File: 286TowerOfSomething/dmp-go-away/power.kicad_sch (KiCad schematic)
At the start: 1 part, among them U1 M6117C

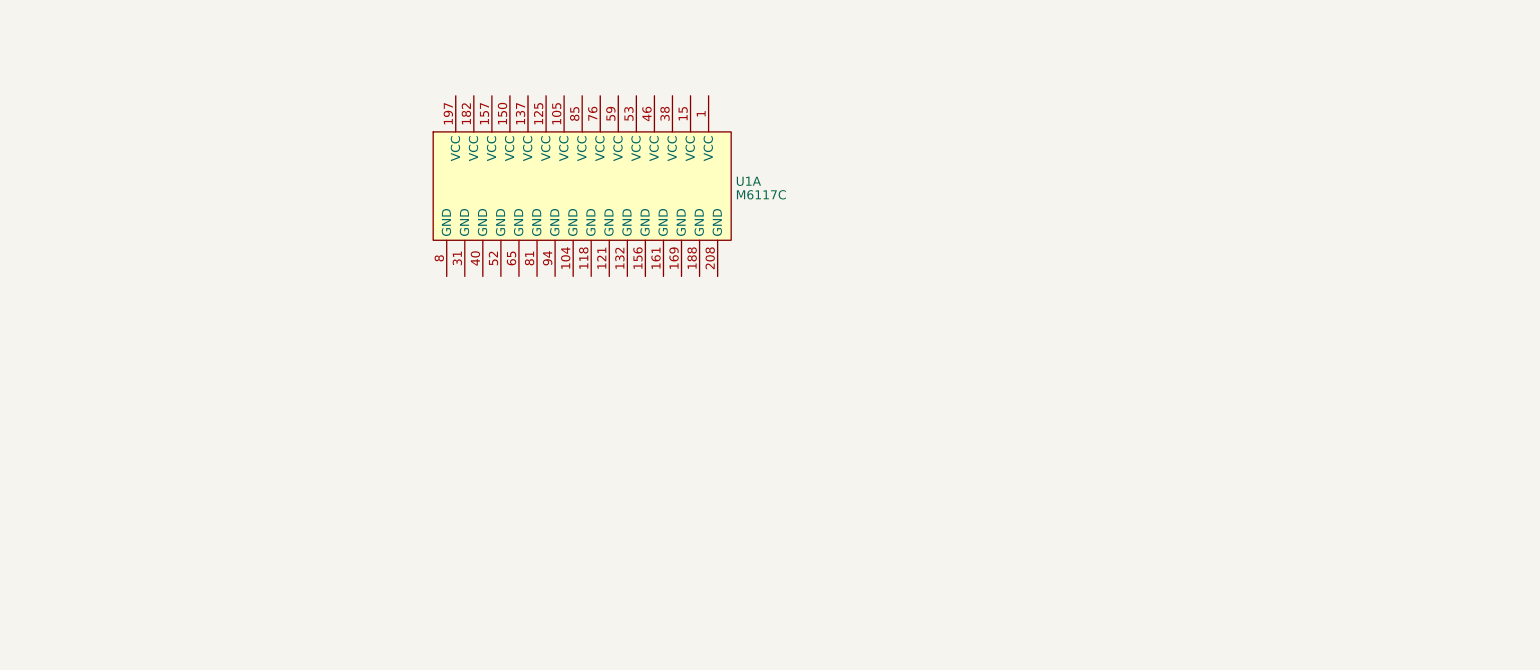
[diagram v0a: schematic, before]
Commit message: Adding work done on 386 card, coming along nicely
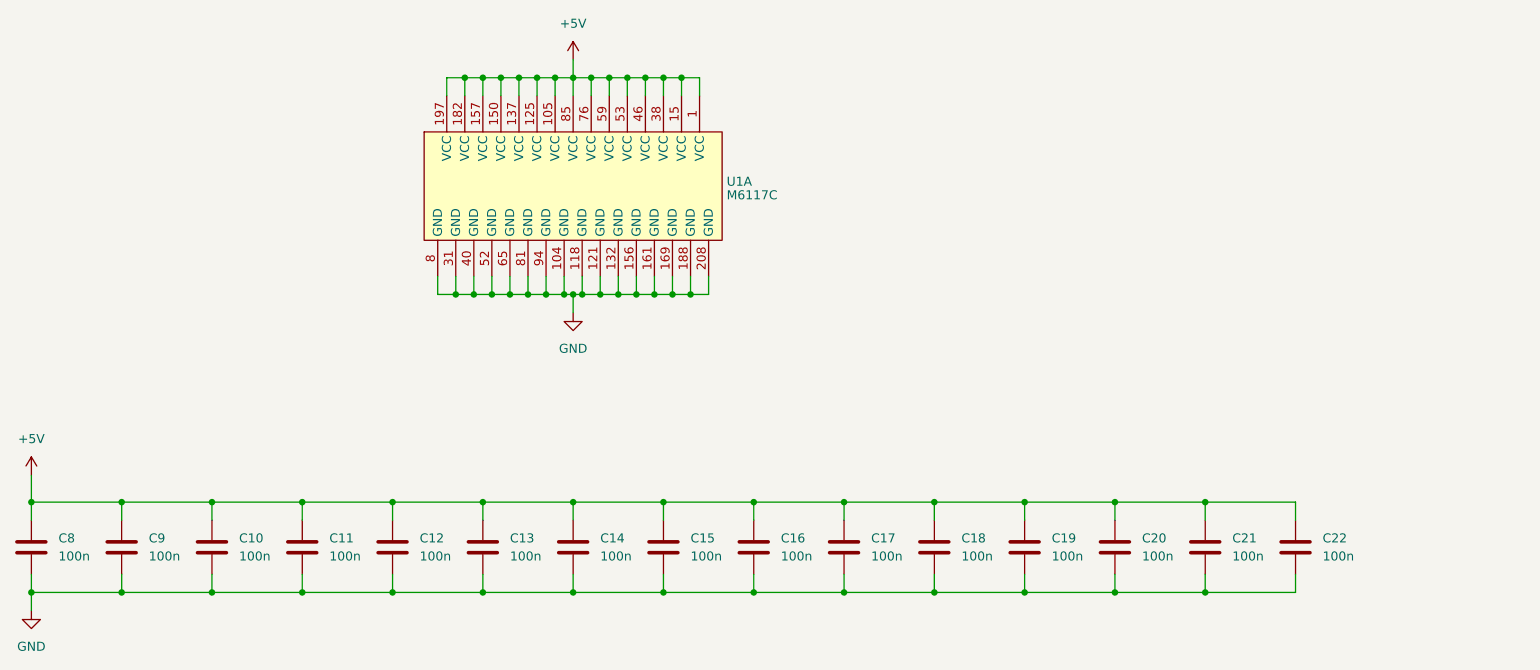
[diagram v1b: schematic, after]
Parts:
- added C10, C11, C12, C13, C14, C15, C16, C17, C18, C19, C20, C21, C22, C8, C9: 100n, symbol Device:C
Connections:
- net +5V: now reaches U1.1 (VCC)
- net +5V: now also U1.105 (VCC), U1.125 (VCC), U1.137 (VCC), U1.15 (VCC), U1.150 (VCC), U1.157 (VCC), U1.182 (VCC), U1.197 (VCC), U1.38 (VCC), U1.46 (VCC), U1.53 (VCC), U1.59 (VCC), U1.76 (VCC), U1.85 (VCC), C10.1, C11.1, C12.1, C13.1, C14.1, C15.1, C16.1, C17.1, C18.1, C19.1, C20.1, C21.1, C22.1, C8.1, C9.1
- net GND: now reaches U1.104 (GND)
- net GND: now also U1.118 (GND), U1.121 (GND), U1.132 (GND), U1.156 (GND), U1.161 (GND), U1.169 (GND), U1.188 (GND), U1.208 (GND), U1.31 (GND), U1.40 (GND), U1.52 (GND), U1.65 (GND), U1.8 (GND), U1.81 (GND), U1.94 (GND), C10.2, C11.2, C12.2, C13.2, C14.2, C15.2, C16.2, C17.2, C18.2, C19.2, C20.2, C21.2, C22.2, C8.2, C9.2
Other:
- moved on the sheet: U1A

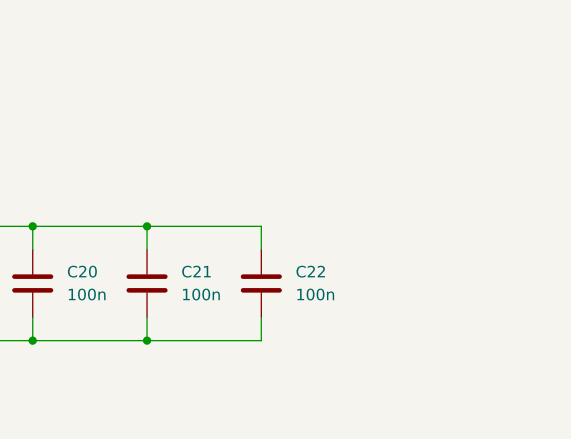
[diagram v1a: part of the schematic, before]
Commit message: Adding some missing caps, and the optional DS12885 RTC for dmp-go-away
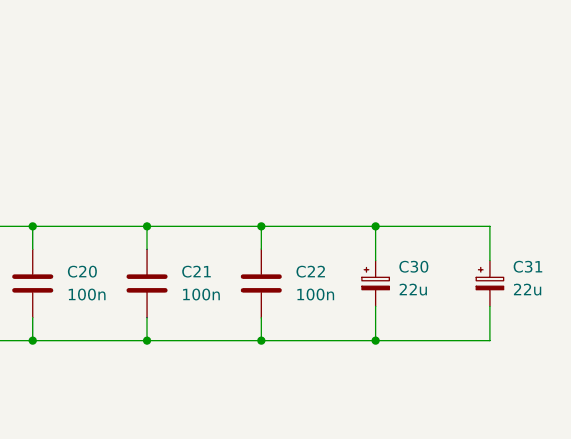
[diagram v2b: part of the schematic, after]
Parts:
- added C30, C31: 22u, symbol Device:C_Polarized_Small
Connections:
- net +5V: now also C30.1, C31.1
- net GND: now also C30.2, C31.2
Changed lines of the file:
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@@
 	(paper "USLetter")
 	(junction
+		(at 228.6 158.75)
+		(diameter 0)
+		(color 0 0 0 0)
+	)
+	(junction
 		(at 127 146.05)
 		(diameter 0)
@@
 	)
 	(junction
+		(at 241.3 146.05)
+		(diameter 0)
+		(color 0 0 0 0)
+	)
+	(junction
 		(at 76.2 158.75)
 		(diameter 0)
@@
 	)
 	(junction
+		(at 228.6 146.05)
+		(diameter 0)
+		(color 0 0 0 0)
+	)
+	(junction
 		(at 114.3 146.05)
 		(diameter 0)
@@
 	)
 	(junction
+		(at 241.3 158.75)
+		(diameter 0)
+		(color 0 0 0 0)
+	)
+	(junction
 		(at 129.54 86.36)
 		(diameter 0)
@@
 	(wire
 		(pts
+			(xy 241.3 146.05) (xy 228.6 146.05)
+		)
+		(stroke
+			(width 0)
+			(type default)
+		)
+	)
+	(wire
+		(pts
 			(xy 228.6 158.75) (xy 228.6 156.21)
 		)
@@
 	(wire
 		(pts
+			(xy 228.6 158.75) (xy 241.3 158.75)
+		)
+		(stroke
+			(width 0)
+			(type default)
+		)
+	)
+	(wire
+		(pts
 			(xy 165.1 156.21) (xy 165.1 158.75)
 		)
@@
 	(wire
 		(pts
+			(xy 254 146.05) (xy 241.3 146.05)
+		)
+		(stroke
+			(width 0)
+			(type default)
+		)
+	)
+	(wire
+		(pts
 			(xy 130.81 114.3) (xy 130.81 116.84)
 		)
@@
 	(wire
 		(pts
+			(xy 241.3 149.86) (xy 241.3 146.05)
+		)
+		(stroke
+			(width 0)
+			(type default)
+		)
+	)
+	(wire
+		(pts
 			(xy 109.22 88.9) (xy 109.22 86.36)
 		)
@@
 	(wire
 		(pts
+			(xy 241.3 158.75) (xy 254 158.75)
+		)
+		(stroke
+			(width 0)
+			(type default)
+		)
+	)
+	(wire
+		(pts
 			(xy 139.7 146.05) (xy 152.4 146.05)
 		)
@@
 	(wire
 		(pts
+			(xy 241.3 158.75) (xy 241.3 154.94)
+		)
+		(stroke
+			(width 0)
+			(type default)
+		)
+	)
+	(wire
+		(pts
 			(xy 127 86.36) (xy 129.54 86.36)
 		)
@@
 	(wire
 		(pts
+			(xy 254 149.86) (xy 254 146.05)
+		)
+		(stroke
+			(width 0)
+			(type default)
+		)
+	)
+	(wire
+		(pts
 			(xy 110.49 114.3) (xy 110.49 116.84)
 		)
@@
 	(wire
 		(pts
+			(xy 254 154.94) (xy 254 158.75)
+		)
+		(stroke
+			(width 0)
+			(type default)
+		)
+	)
+	(wire
+		(pts
 			(xy 119.38 86.36) (xy 119.38 88.9)
 		)
@@
 	)
 	(symbol
+		(lib_id "Device:C_Polarized_Small")
+		(at 241.3 152.4 0)
+		(unit 1)
+		(exclude_from_sim no)
+		(in_bom yes)
+		(on_board yes)
+		(dnp no)
+		(fields_autoplaced yes)
+		(property "Reference" "C30"
+			(at 243.84 150.5838 0)
+			(effects
+				(font
+					(size 1.27 1.27)
+				)
+				(justify left)
+			)
+		)
+		(property "Value" "22u"
+			(at 243.84 153.1238 0)
+			(effects
+				(font
+					(size 1.27 1.27)
+				)
+				(justify left)
+			)
+		)
+		(property "Footprint" ""
+			(at 241.3 152.4 0)
+			(effects
+				(font
+					(size 1.27 1.27)
+				)
+				(hide yes)
+			)
+		)
+		(property "Datasheet" "~"
+			(at 241.3 152.4 0)
+			(effects
+				(font
+					(size 1.27 1.27)
+				)
+				(hide yes)
+			)
+		)
+		(property "Description" "Polarized capacitor, small symbol"
+			(at 241.3 152.4 0)
+			(effects
+				(font
+					(size 1.27 1.27)
+				)
+				(hide yes)
+			)
+		)
+		(pin "2"
+		)
+		(pin "1"
+		)
+		(instances
+			(project ""
+				(path "/b66cfc40-8652-41e7-bd5f-f23cb0cb78db/de3f85e5-98cb-47f6-9751-2a5a4919266b"
+					(reference "C30")
+					(unit 1)
+				)
+			)
+		)
+	)
+	(symbol
 		(lib_id "power:+5V")
 		(at 127 83.82 0)
@@
 					(unit 1)
 				)
+			)
+		)
+	)
+	(symbol
+		(lib_id "Device:C_Polarized_Small")
+		(at 254 152.4 0)
+		(unit 1)
+		(exclude_from_sim no)
+		(in_bom yes)
+		(on_board yes)
+		(dnp no)
+		(fields_autoplaced yes)
+		(property "Reference" "C31"
+			(at 256.54 150.5838 0)
+			(effects
+				(font
+					(size 1.27 1.27)
+				)
+				(justify left)
+			)
+		)
+		(property "Value" "22u"
+			(at 256.54 153.1238 0)
+			(effects
+				(font
+					(size 1.27 1.27)
+				)
+				(justify left)
+			)
+		)
+		(property "Footprint" ""
+			(at 254 152.4 0)
+			(effects
+				(font
+					(size 1.27 1.27)
+				)
+				(hide yes)
+			)
+		)
+		(property "Datasheet" "~"
+			(at 254 152.4 0)
+			(effects
+				(font
+					(size 1.27 1.27)
+				)
+				(hide yes)
+			)
+		)
+		(property "Description" "Polarized capacitor, small symbol"
+			(at 254 152.4 0)
+			(effects
+				(font
+					(size 1.27 1.27)
+				)
+				(hide yes)
+			)
+		)
+		(pin "2"
+		)
+		(pin "1"
+		)
+		(instances
+			(project "dmp-go-away"
+				(path "/b66cfc40-8652-41e7-bd5f-f23cb0cb78db/de3f85e5-98cb-47f6-9751-2a5a4919266b"
+					(reference "C31")
+					(unit 1)
+				)

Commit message: Added footprints and started figuring out layout for dmp-go-away
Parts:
- C10, C11, C12, C13, C14, C15, C16, C17, C18, C19, C20, C21, C22, C8, C9: footprint (none) -> Capacitor_SMD:C_0603_1608Metric_Pad1.08x0.95mm_HandSolder
- C30, C31: footprint (none) -> Capacitor_SMD:CP_Elec_5x5.3
- U1: footprint (none) -> Package_QFP:PQFP-208_28x28mm_P0.5mm
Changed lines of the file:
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@@
 			)
 		)
-		(property "Footprint" ""
+		(property "Footprint" "Capacitor_SMD:C_0603_1608Metric_Pad1.08x0.95mm_HandSolder"
 			(at 77.1652 156.21 0)
 			(effects
@@
 			)
 		)
-		(property "Footprint" ""
+		(property "Footprint" "Capacitor_SMD:C_0603_1608Metric_Pad1.08x0.95mm_HandSolder"
 			(at 115.2652 156.21 0)
 			(effects
@@
 			)
 		)
-		(property "Footprint" ""
+		(property "Footprint" "Capacitor_SMD:C_0603_1608Metric_Pad1.08x0.95mm_HandSolder"
 			(at 178.7652 156.21 0)
 			(effects
@@
 			)
 		)
-		(property "Footprint" ""
+		(property "Footprint" "Capacitor_SMD:C_0603_1608Metric_Pad1.08x0.95mm_HandSolder"
 			(at 51.7652 156.21 0)
 			(effects
@@
 			)
 		)
-		(property "Footprint" ""
+		(property "Footprint" "Capacitor_SMD:C_0603_1608Metric_Pad1.08x0.95mm_HandSolder"
 			(at 102.5652 156.21 0)
 			(effects
@@
 			)
 		)
-		(property "Footprint" ""
+		(property "Footprint" "Package_QFP:PQFP-208_28x28mm_P0.5mm"
 			(at 127 101.6 0)
 			(effects
@@
 			)
 		)
-		(property "Footprint" ""
+		(property "Footprint" "Capacitor_SMD:C_0603_1608Metric_Pad1.08x0.95mm_HandSolder"
 			(at 127.9652 156.21 0)
 			(effects
@@
 			)
 		)
-		(property "Footprint" ""
+		(property "Footprint" "Capacitor_SMD:C_0603_1608Metric_Pad1.08x0.95mm_HandSolder"
 			(at 216.8652 156.21 0)
 			(effects
@@
 			)
 		)
-		(property "Footprint" ""
+		(property "Footprint" "Capacitor_SMD:C_0603_1608Metric_Pad1.08x0.95mm_HandSolder"
 			(at 166.0652 156.21 0)
 			(effects
@@
 			)
 		)
-		(property "Footprint" ""
+		(property "Footprint" "Capacitor_SMD:C_0603_1608Metric_Pad1.08x0.95mm_HandSolder"
 			(at 229.5652 156.21 0)
 			(effects
@@
 			)
 		)
-		(property "Footprint" ""
+		(property "Footprint" "Capacitor_SMD:C_0603_1608Metric_Pad1.08x0.95mm_HandSolder"
 			(at 89.8652 156.21 0)
 			(effects
@@
 			)
 		)
-		(property "Footprint" ""
+		(property "Footprint" "Capacitor_SMD:C_0603_1608Metric_Pad1.08x0.95mm_HandSolder"
 			(at 140.6652 156.21 0)
 			(effects
@@
 			)
 		)
-		(property "Footprint" ""
+		(property "Footprint" "Capacitor_SMD:CP_Elec_5x5.3"
 			(at 241.3 152.4 0)
 			(effects
@@
 			)
 		)
-		(property "Footprint" ""
+		(property "Footprint" "Capacitor_SMD:C_0603_1608Metric_Pad1.08x0.95mm_HandSolder"
 			(at 153.3652 156.21 0)
 			(effects
@@
 			)
 		)
-		(property "Footprint" ""
+		(property "Footprint" "Capacitor_SMD:C_0603_1608Metric_Pad1.08x0.95mm_HandSolder"
 			(at 204.1652 156.21 0)
 			(effects
@@
 			)
 		)
-		(property "Footprint" ""
+		(property "Footprint" "Capacitor_SMD:CP_Elec_5x5.3"
 			(at 254 152.4 0)
 			(effects
@@
 			)
 		)
-		(property "Footprint" ""
+		(property "Footprint" "Capacitor_SMD:C_0603_1608Metric_Pad1.08x0.95mm_HandSolder"
 			(at 64.4652 156.21 0)
 			(effects
@@
 			)
 		)
-		(property "Footprint" ""
+		(property "Footprint" "Capacitor_SMD:C_0603_1608Metric_Pad1.08x0.95mm_HandSolder"
 			(at 191.4652 156.21 0)
 			(effects
